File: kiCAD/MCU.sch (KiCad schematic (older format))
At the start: 52 parts

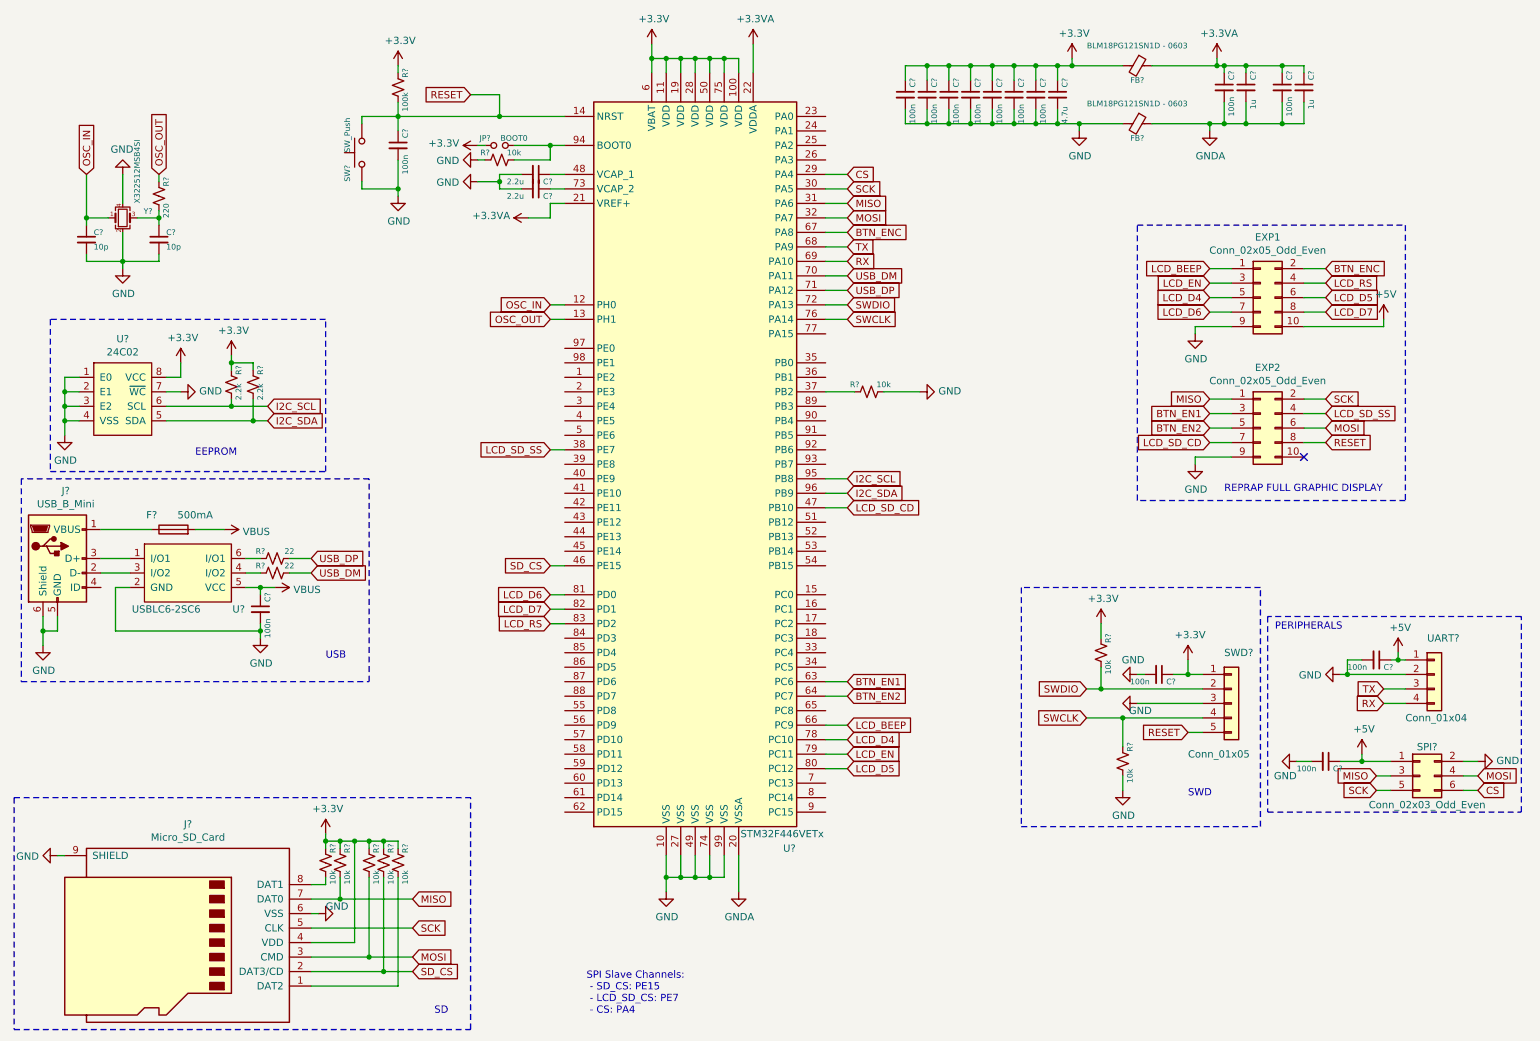
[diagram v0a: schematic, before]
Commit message: Completed Schematic, assigned footprints.
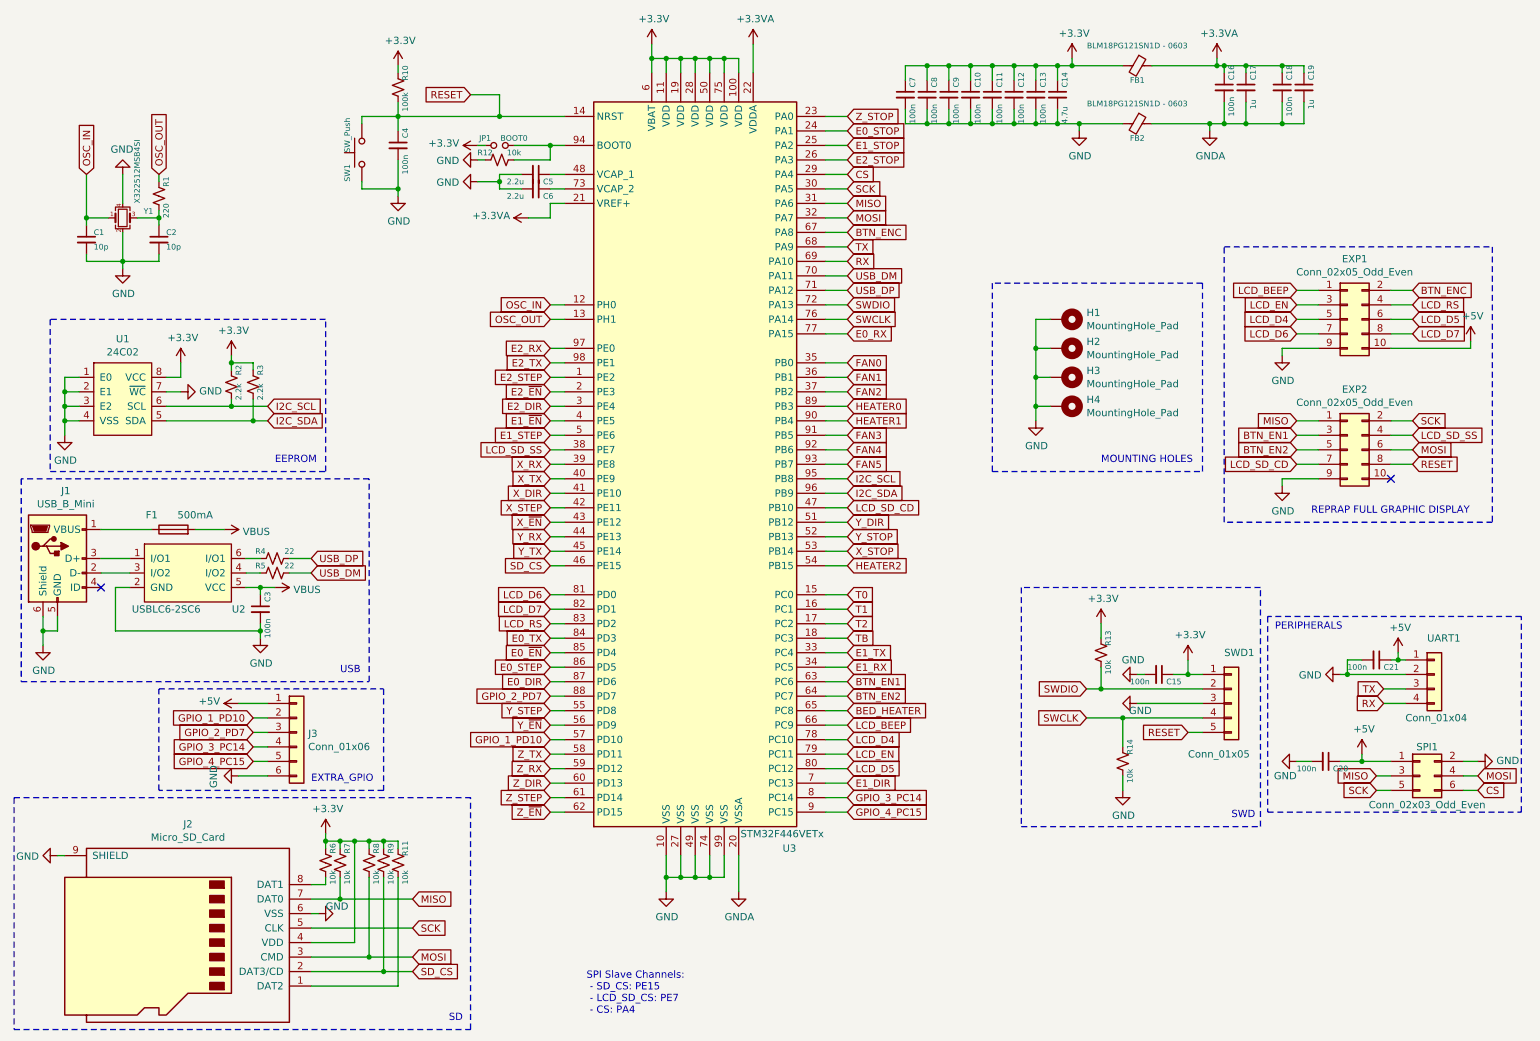
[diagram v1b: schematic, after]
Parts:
- removed R?: 10k, symbol Device:R_Small_US
- added H1, H2, H3, H4: MountingHole_Pad, MountingHole:MountingHole_4.3mm_M4_Pad_Via, symbol Mechanical:MountingHole_Pad
- added J3: Conn_01x06, Connector_PinSocket_2.54mm:PinSocket_1x06_P2.54mm_Vertical, symbol Connector_Generic:Conn_01x06
- C1, C10, C11, C12, C13, C14, C15, C16, C17, C18, C19, C2, C20, C21, C3, C4, C7, C8, C9: renamed from C?; footprint (none) -> Capacitor_SMD:C_0603_1608Metric_Pad1.05x0.95mm_HandSolder
- C5, C6: renamed from C?; footprint (none) -> Capacitor_SMD:C_0805_2012Metric_Pad1.15x1.40mm_HandSolder
- EXP1, EXP2: footprint (none) -> Connector_PinHeader_2.54mm:PinHeader_2x05_P2.54mm_Vertical
- F1: renamed from F?; footprint (none) -> Fuse:Fuse_1812_4532Metric_Pad1.30x3.40mm_HandSolder
- FB1, FB2: renamed from FB?; footprint (none) -> Resistor_SMD:R_0201_0603Metric
- J1: renamed from J?; footprint (none) -> Connector_USB:USB_Mini-B_Lumberg_2486_01_Horizontal
- J2: renamed from J?; footprint (none) -> Connector_Card:microSD_HC_Wuerth_693072010801
- JP1: renamed from JP?; footprint (none) -> Connector_PinHeader_2.54mm:PinHeader_1x02_P2.54mm_Vertical
- R1, R10, R11, R12, R13, R14, R2, R3, R4, R5, R6, R7, R8, R9: renamed from R?; footprint (none) -> Resistor_SMD:R_0603_1608Metric_Pad1.05x0.95mm_HandSolder
- SPI1: renamed from SPI?; footprint (none) -> Connector_PinHeader_2.54mm:PinHeader_2x03_P2.54mm_Vertical
- SW1: renamed from SW?; footprint (none) -> Button_Switch_SMD:SW_Push_1P1T_NO_6x6mm_H9.5mm
- SWD1: renamed from SWD?; footprint (none) -> Connector_PinHeader_2.54mm:PinHeader_1x05_P2.54mm_Vertical
- U1: renamed from U?; footprint (none) -> Package_SO:SOIC-8_3.9x4.9mm_P1.27mm
- U2: renamed from U?; footprint (none) -> Package_TO_SOT_SMD:SOT-23-6_Handsoldering
- UART1: renamed from UART?; footprint (none) -> Connector_PinHeader_2.54mm:PinHeader_1x04_P2.54mm_Vertical
- Y1: renamed from Y?; footprint (none) -> Crystal:Crystal_SMD_3225-4Pin_3.2x2.5mm_HandSoldering
- gave numbers to parts that had none: 1
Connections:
- net +5V: now also J3.1 (Pin_1)
- net GND: now also H1.1, H2.1, H3.1, H4.1, J3.6 (Pin_6)
- net E2_STEP: now reaches U3.1 (PE2)
- net T0: now reaches U3.15 (PC0)
- net T1: now reaches U3.16 (PC1)
- net T2: now reaches U3.17 (PC2)
- net TB: now reaches U3.18 (PC3)
- net E2_~EN: now reaches U3.2 (PE3)
- net Z_STOP: now reaches U3.23 (PA0)
- net E0_STOP: now reaches U3.24 (PA1)
- net E1_STOP: now reaches U3.25 (PA2)
- net E2_STOP: now reaches U3.26 (PA3)
- net E2_DIR: now reaches U3.3 (PE4)
- net E1_TX: now reaches U3.33 (PC4)
- net E1_RX: now reaches U3.34 (PC5)
- net FAN0: now reaches U3.35 (PB0)
- net FAN1: now reaches U3.36 (PB1)
- net FAN2: now reaches U3.37 (PB2)
- net X_RX: now reaches U3.39 (PE8)
- net E1_~EN: now reaches U3.4 (PE5)
- net X_TX: now reaches U3.40 (PE9)
- net X_DIR: now reaches U3.41 (PE10)
- net X_STEP: now reaches U3.42 (PE11)
- net X_~EN: now reaches U3.43 (PE12)
- net Y_RX: now reaches U3.44 (PE13)
- net Y_TX: now reaches U3.45 (PE14)
- net E1_STEP: now reaches U3.5 (PE6)
- net Y_DIR: now reaches U3.51 (PB12)
- net Y_STOP: now reaches U3.52 (PB13)
- net X_STOP: now reaches U3.53 (PB14)
- net HEATER2: now reaches U3.54 (PB15)
- net Y_STEP: now reaches U3.55 (PD8)
- net Y_~EN: now reaches U3.56 (PD9)
- net GPIO_1_PD10: now reaches U3.57 (PD10)
- net GPIO_1_PD10: now also J3.2 (Pin_2)
- net Z_TX: now reaches U3.58 (PD11)
- net Z_RX: now reaches U3.59 (PD12)
- net Z_DIR: now reaches U3.60 (PD13)
- net Z_STEP: now reaches U3.61 (PD14)
- net Z_~EN: now reaches U3.62 (PD15)
- net BED_HEATER: now reaches U3.65 (PC8)
- net E1_DIR: now reaches U3.7 (PC13)
- net E0_RX: now reaches U3.77 (PA15)
- net GPIO_3_PC14: now reaches U3.8 (PC14)
- net GPIO_3_PC14: now also J3.4 (Pin_4)
- net E0_TX: now reaches U3.84 (PD3)
- net E0_~EN: now reaches U3.85 (PD4)
- net E0_STEP: now reaches U3.86 (PD5)
- net E0_DIR: now reaches U3.87 (PD6)
- net GPIO_2_PD7: now reaches U3.88 (PD7)
- net GPIO_2_PD7: now also J3.3 (Pin_3)
- net HEATER0: now reaches U3.89 (PB3)
- net GPIO_4_PC15: now reaches U3.9 (PC15)
- net GPIO_4_PC15: now also J3.5 (Pin_5)
- net HEATER1: now reaches U3.90 (PB4)
- net FAN3: now reaches U3.91 (PB5)
- net FAN4: now reaches U3.92 (PB6)
- net FAN5: now reaches U3.93 (PB7)
- net E2_RX: now reaches U3.97 (PE0)
- net E2_TX: now reaches U3.98 (PE1)
- no-connect marks 1 -> 2
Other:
- note added: "EXTRA_GPIO\n"
- note added: "MOUNTING HOLES\n"
- moved on the sheet: EXP1, EXP2

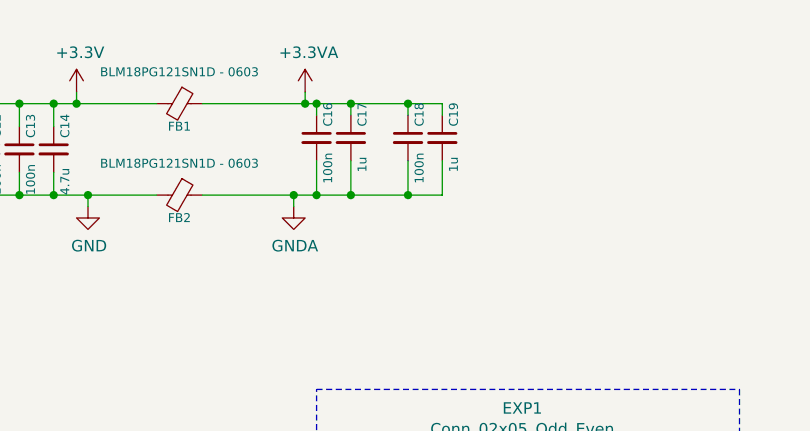
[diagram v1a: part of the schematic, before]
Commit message: finished layout of everything but endstops.
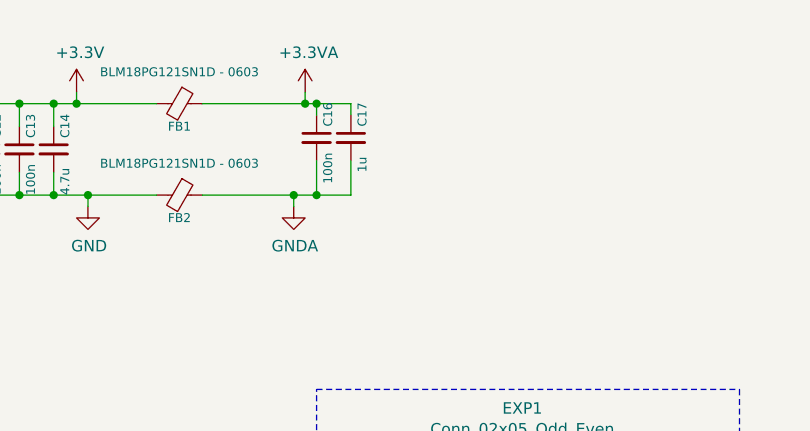
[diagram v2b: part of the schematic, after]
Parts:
- removed C18: 100n, Capacitor_SMD:C_0603_1608Metric_Pad1.05x0.95mm_HandSolder, symbol Device:C_Small
- removed C19: 1u, Capacitor_SMD:C_0603_1608Metric_Pad1.05x0.95mm_HandSolder, symbol Device:C_Small
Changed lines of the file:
@@
-$EndComp
-$Comp
-L Device:C_Small C18
-U 1 1 5FAEA53B
-P 9500 1150
-F 0 "C18" V 9550 1200 39  0000 L CNN
-F 1 "100n" V 9550 950 39  0000 L CNN
-F 2 "Capacitor_SMD:C_0603_1608Metric_Pad1.05x0.95mm_HandSolder" H 9500 1150 50  0001 C CNN
-F 3 "~" H 9500 1150 50  0001 C CNN
-	1    9500 1150
-	1    0    0    -1
 $EndComp
 $Comp
@@
 F 3 "~" H 9250 1150 50  0001 C CNN
 	1    9250 1150
-	1    0    0    -1
-$EndComp
-$Comp
-L Device:C_Small C19
-U 1 1 5FAEABE3
-P 9650 1150
-F 0 "C19" V 9700 1200 39  0000 L CNN
-F 1 "1u" V 9700 1000 39  0000 L CNN
-F 2 "Capacitor_SMD:C_0603_1608Metric_Pad1.05x0.95mm_HandSolder" H 9650 1150 50  0001 C CNN
-F 3 "~" H 9650 1150 50  0001 C CNN
-	1    9650 1150
 	1    0    0    -1
 $EndComp
@@
 	9250 1000 9250 1050
 Wire Wire Line
-	9500 1050 9500 1000
-Wire Wire Line
-	9500 1000 9650 1000
-Wire Wire Line
-	9650 1000 9650 1050
-Wire Wire Line
-	9650 1250 9650 1400
-Wire Wire Line
-	9650 1400 9500 1400
-Wire Wire Line
-	9500 1400 9500 1250
-Wire Wire Line
-	9250 1000 9500 1000
-Connection ~ 9250 1000
-Connection ~ 9500 1000
-Wire Wire Line
-	9500 1400 9250 1400
-Connection ~ 9500 1400
-Connection ~ 9250 1400
-Wire Wire Line
 	9050 1000 9100 1000
